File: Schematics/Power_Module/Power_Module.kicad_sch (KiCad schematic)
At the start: 131 parts, among them J1 ScrewSwitch B, J2 ScrewSwitch A, J3 Battery A, J4 USB_C_Female_USB2_Small, J5 Battery B, J6 Stack Male Edge Connector, J7 SWD_B, J8 SWD_B, Q1 AO4447A, Q2 AO4447A, U1 LMR51430XDDCR, U10 ISO1042BDWVR, U11 LM66100DCKR, U12 LM66100DCKR, U13 LM66100DCKR, U14 LM66100DCKR, U15 LM66100DCKR, U16 SCM3721ASA, U2 LMR51430XDDCR, U3 LMR51430XDDCR, U4 STM32F103C8Tx, U5 STM32F103C8Tx, U6 ACS37041KLHBLT-010B3, U7 ACS37041KLHBLT-010B3, U8 ACS37041KLHBLT-010B3, U9 AMS1117-3.3, Y1 X322516MMB4SI

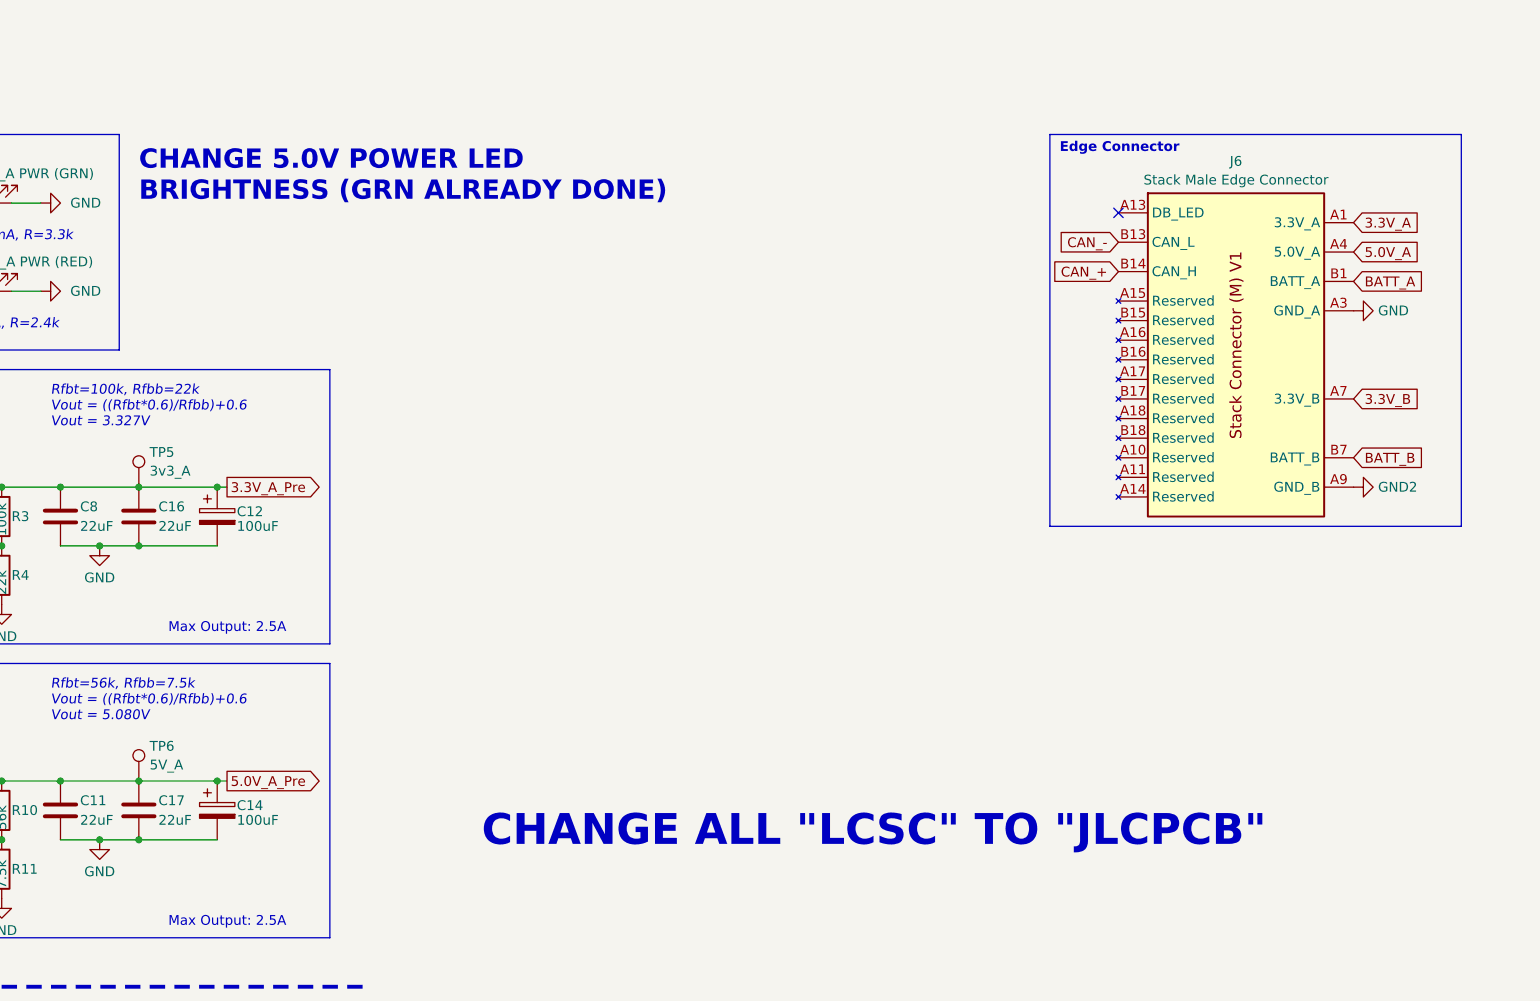
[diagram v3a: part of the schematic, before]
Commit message: Changed "LCSC" fields to "JLCPCB"
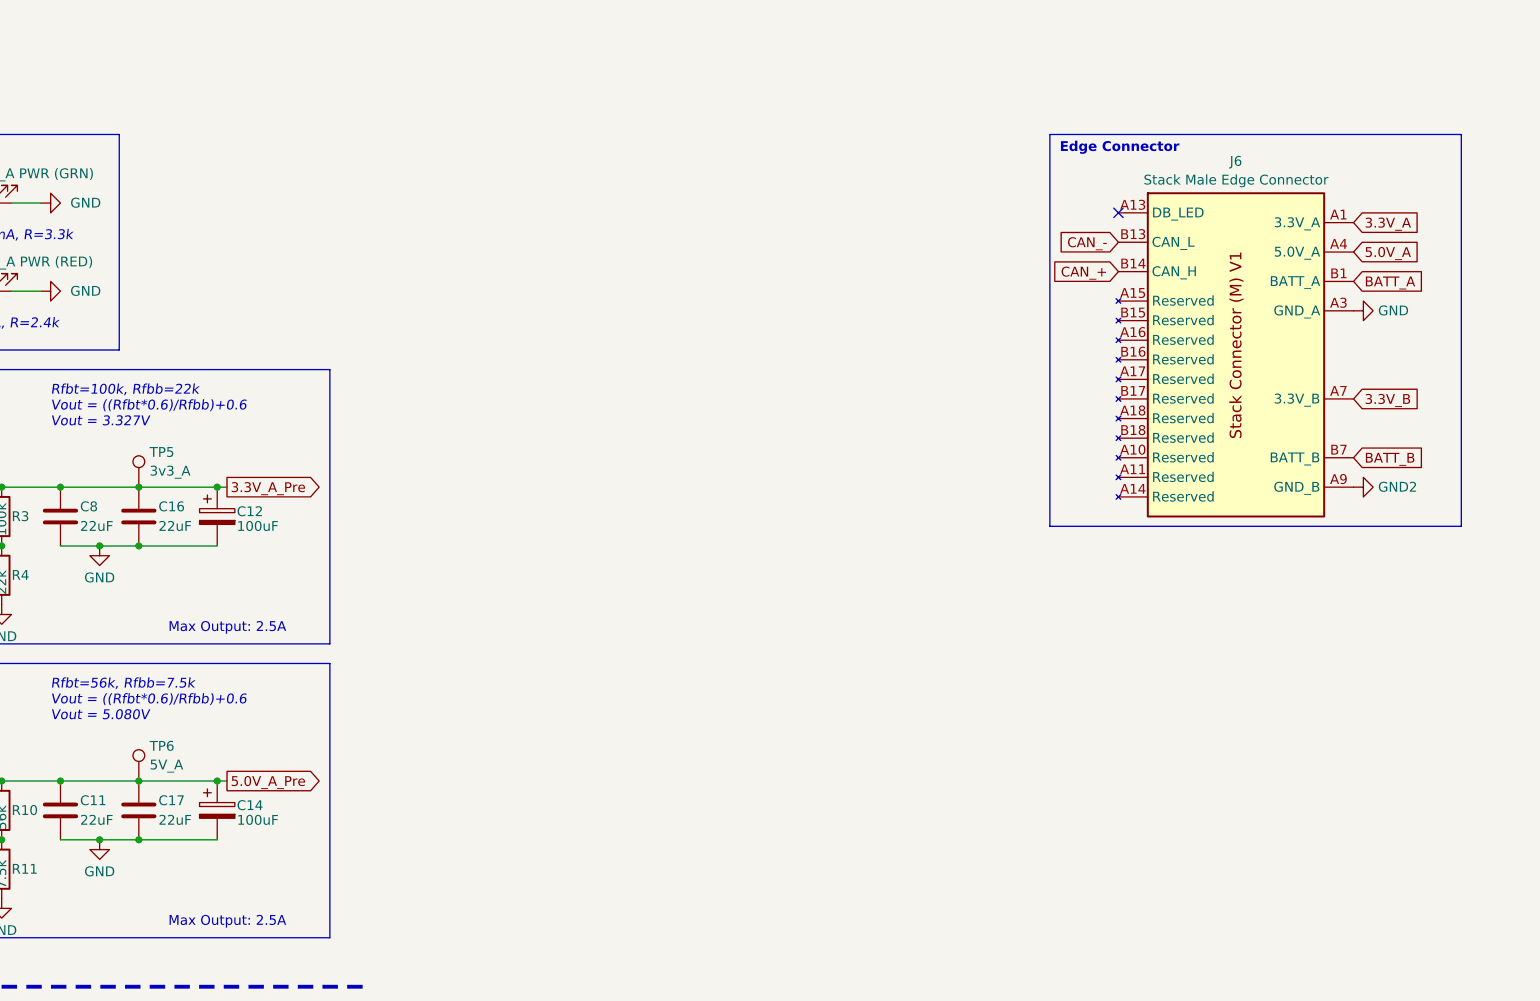
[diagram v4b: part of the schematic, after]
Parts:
- C1, C2, C3: JLCPCB (none) -> C1779; LCSC C1779 -> (none)
- C10, C21, C22, C4, C44, C45, C46, C47, C48, C49, C5, C50, C6, C7, C9: JLCPCB (none) -> C14663; LCSC C14663 -> (none)
- C11, C13, C16, C17, C18, C8: JLCPCB (none) -> C45783; LCSC C45783 -> (none)
- C19, C20: JLCPCB (none) -> C96446; LCSC C96446 -> (none)
- C23, C24: JLCPCB (none) -> C1634; LCSC C1634 -> (none)
- C25, C26, C27, C28, C29, C30, C31, C32: JLCPCB (none) -> C1525; LCSC C1525 -> (none)
- C33, C36: JLCPCB (none) -> C57112; LCSC C57112 -> (none)
- C34, C35, C37, C38: JLCPCB (none) -> C28323; LCSC C28323 -> (none)
- C39, C40, C41, C42, C43: JLCPCB (none) -> C15849; LCSC C15849 -> (none)
- D1, D3: JLCPCB (none) -> C2297; LCSC C2297 -> (none)
- D2: JLCPCB (none) -> C84256; LCSC C84256 -> (none)
- D5, D8: JLCPCB (none) -> C72038; LCSC C72038 -> (none)
- FB1, FB2: JLCPCB (none) -> C1015; LCSC C1015 -> (none)
- J4: JLCPCB (none) -> C2936184; LCSC C2936184 -> (none)
- Q1, Q2: JLCPCB (none) -> C125867; LCSC C125867 -> (none)
- R1, R23, R25, R26, R28, R3: JLCPCB (none) -> C25803; LCSC C25803 -> (none)
- R10: JLCPCB (none) -> C23206; LCSC C23206 -> (none)
- R11: JLCPCB (none) -> C23234; LCSC C23234 -> (none)
- R12, R5: JLCPCB (none) -> C22984; LCSC C22984 -> (none)
- R13, R15, R21, R22, R6: JLCPCB (none) -> C25804; LCSC C25804 -> (none)
- R16: JLCPCB (none) -> C22843; LCSC C22843 -> (none)
- R17, R18: JLCPCB (none) -> C23186; LCSC C23186 -> (none)
- R19, R20: JLCPCB (none) -> C23228; LCSC C23228 -> (none)
- R2, R4: JLCPCB (none) -> C31850; LCSC C31850 -> (none)
- R7, R9: JLCPCB (none) -> C22978; LCSC C22978 -> (none)
- R8: JLCPCB (none) -> C22940; LCSC C22940 -> (none)
- U10: JLCPCB (none) -> C484409; LCSC C484409 -> (none)
- U11, U12, U13, U14, U15: JLCPCB (none) -> C2869734; LCSC C2869734 -> (none)
- U9: JLCPCB (none) -> C6186; LCSC C6186 -> (none)
- Y1: JLCPCB (none) -> C13738; LCSC C13738 -> (none)
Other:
- note removed: "CHANGE 5.0V POWER LED BRIGHTNESS (GRN ALREADY DONE)"
- note removed: "CHANGE ALL "LCSC" TO "JLCPCB""

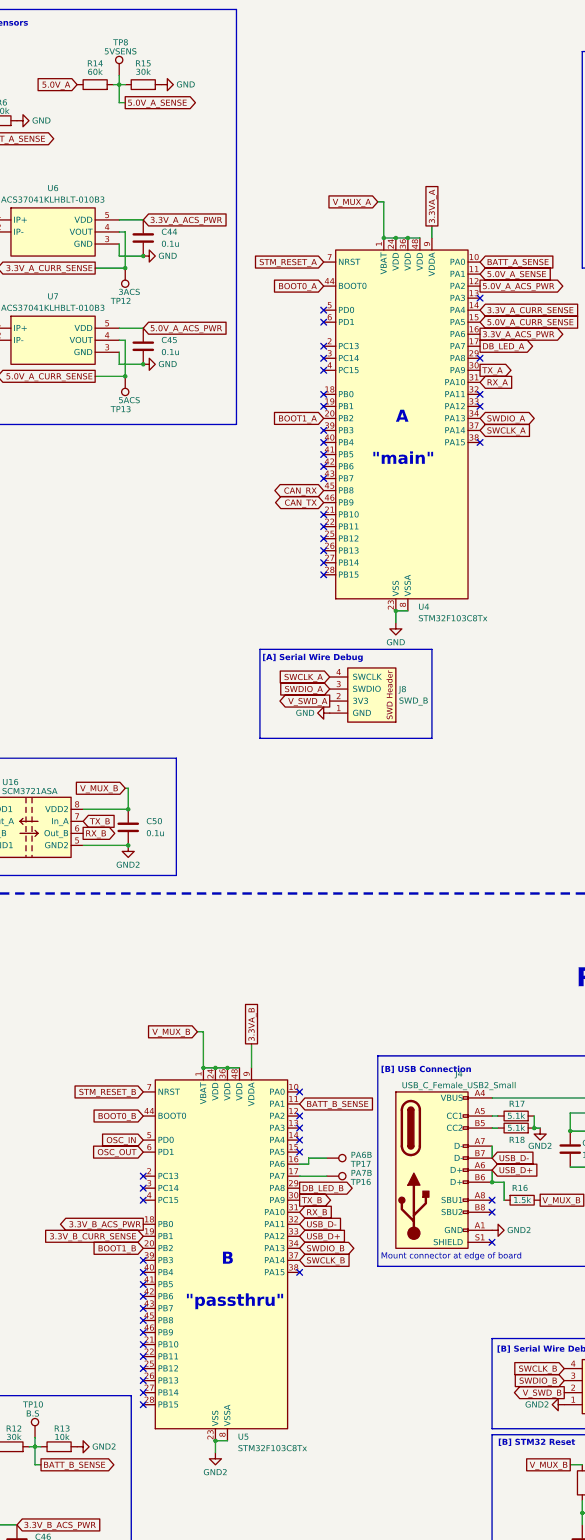
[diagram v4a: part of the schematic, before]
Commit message: Added/fixed part numbers
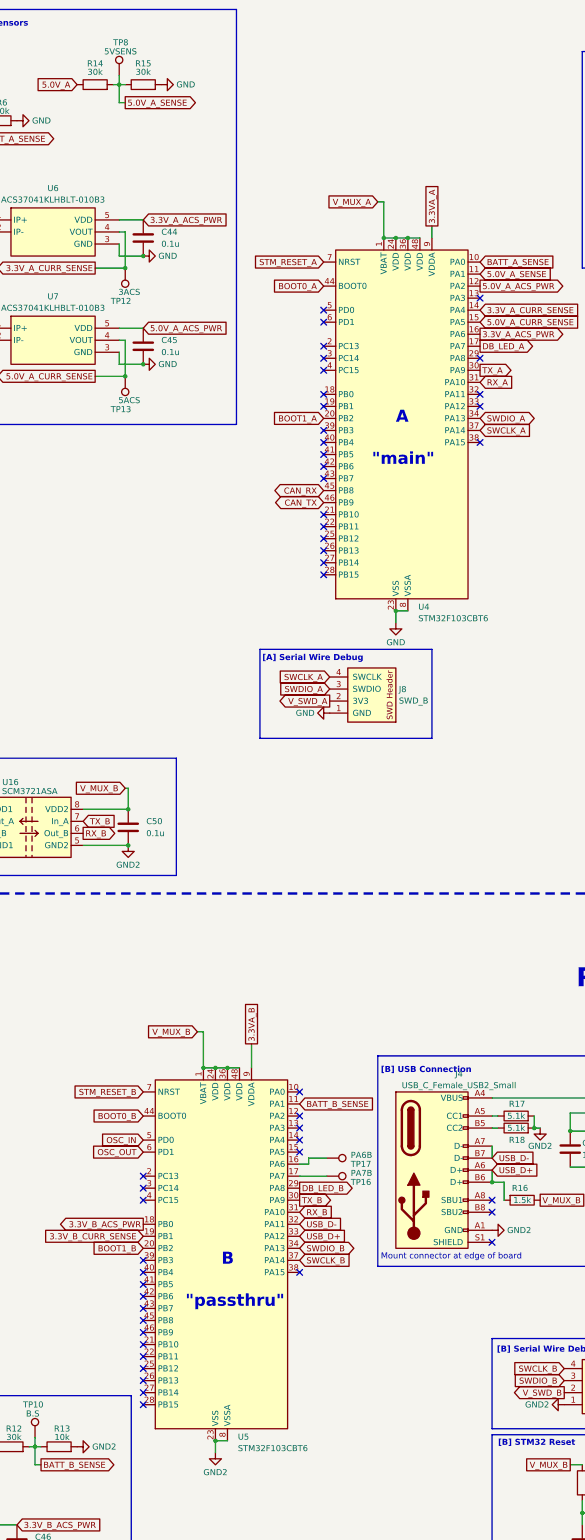
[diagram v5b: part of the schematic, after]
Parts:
- R14: value 60k -> 30k; JLCPCB (none) -> C22984
- R15: JLCPCB C25804 -> C22984
- U16: Digikey (none) -> 2725-SCM3721ASACT-ND
- U4, U5: value STM32F103C8Tx -> STM32F103CBT6; JLCPCB (none) -> C8304
- U6, U7, U8: Digikey (none) -> 620-ACS37041KLHBLT-010B3CT-ND
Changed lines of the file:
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@@
       (effects (font (size 1.27 1.27)) (justify left top) hide)
     )
+    (property "Digikey" "620-ACS37041KLHBLT-010B3CT-ND" (at 300.99 254 0)
+      (effects (font (size 1.27 1.27)) hide)
+    )
     (pin "1")
     (pin "2")
@@
       (effects (font (size 1.27 1.27)) (justify left top) hide)
     )
+    (property "Digikey" "620-ACS37041KLHBLT-010B3CT-ND" (at 327.66 1.27 0)
+      (effects (font (size 1.27 1.27)) hide)
+    )
     (pin "1")
     (pin "2")
@@
       (effects (font (size 1.27 1.27)) hide)
     )
-    (property "JLCPCB" "C25804" (at 360.68 -50.165 90)
+    (property "JLCPCB" "C22984" (at 360.68 -50.165 90)
       (effects (font (size 1.27 1.27)) hide)
     )
@@
       (effects (font (size 1.27 1.27)) hide)
     )
+    (property "Digikey" "2725-SCM3721ASACT-ND" (at 336.55 99.06 0)
+      (effects (font (size 1.27 1.27)) hide)
+    )
     (pin "1")
     (pin "2")
@@
       (effects (font (size 1.27 1.27)) (justify left))
     )
-    (property "Value" "STM32F103C8Tx" (at 380.6541 237.8243 0)
+    (property "Value" "STM32F103CBT6" (at 380.6541 237.8243 0)
       (effects (font (size 1.27 1.27)) (justify left))
     )
@@
       (effects (font (size 1.27 1.27)) hide)
     )
+    (property "JLCPCB" "C8304" (at 375.92 198.12 0)
+      (effects (font (size 1.27 1.27)) hide)
+    )
     (pin "1")
     (pin "10")
@@
       (effects (font (size 1.27 1.27)) (justify left top) hide)
     )
+    (property "Digikey" "620-ACS37041KLHBLT-010B3CT-ND" (at 327.66 -21.59 0)
+      (effects (font (size 1.27 1.27)) hide)
+    )
     (pin "1")
     (pin "2")
@@
       (effects (font (size 1.27 1.27)) (justify left))
     )
-    (property "Value" "STM32F103C8Tx" (at 418.7541 62.5643 0)
+    (property "Value" "STM32F103CBT6" (at 418.7541 62.5643 0)
       (effects (font (size 1.27 1.27)) (justify left))
     )
@@
       (effects (font (size 1.27 1.27)) hide)
     )
+    (property "JLCPCB" "C8304" (at 414.02 22.86 0)
+      (effects (font (size 1.27 1.27)) hide)
+    )
     (pin "1")
     (pin "10")
@@
       (effects (font (size 1.27 1.27)))
     )
-    (property "Value" "60k" (at 350.52 -52.8208 90)
+    (property "Value" "30k" (at 350.52 -52.8208 90)
       (effects (font (size 1.27 1.27)))
     )
@@
       (effects (font (size 1.27 1.27)) hide)
     )
-    (property "JLCPCB" "" (at 350.52 -50.165 90)
+    (property "JLCPCB" "C22984" (at 350.52 -50.165 90)
       (effects (font (size 1.27 1.27)) hide)
     )

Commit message: Tweaked some part numbers
-Changed STM32F103CB to STM32F103C8
-Changed USB port to C5178541
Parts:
- J4: JLCPCB C2936184 -> C5178541
- U4, U5: value STM32F103CBT6 -> STM32F103C8T6; JLCPCB C8304 -> C8734
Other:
- note removed: "DONT BE AFRAID TO MOUNT STUFF ON BOTTOM LAYER, SO LONG AS ITS MANUALLY INSTALLED"
- note removed: "This module is already going to be very different from a standard module. It does not have to be as user-friendly; it already doesn't have reset/boot buttons. Maybe remove most LMR66100s and only add ones to prevent it from back-powering the entire stack."
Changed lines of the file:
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@@
     (effects (font (size 4 4) (thickness 0.8) bold) (justify left bottom))
   )
-  (text "This module is already going to be\nvery different from a standard\nmodule. It does not have to be\nas user-friendly; it already doesn't\nhave reset/boot buttons.\n\nMaybe remove most LMR66100s and only\nadd ones to prevent it from back-powering\nthe entire stack."
-    (at 571.5 306.705 0)
-    (effects (font (size 4 4) (thickness 0.8) bold) (justify left bottom))
-  )
   (text "[B] STM32 Decoupling Capacitors for VBAT/VDD" (at 485.14 203.835 0)
     (effects (font (size 1.27 1.27) (thickness 0.254) bold) (justify left bottom))
@@
     (effects (font (size 1.27 1.27) (thickness 0.254) bold) (justify left bottom))
   )
-  (text "DONT BE AFRAID TO MOUNT STUFF ON BOTTOM\nLAYER, SO LONG AS ITS MANUALLY INSTALLED"
-    (at 262.89 299.085 0)
-    (effects (font (size 4 4) (thickness 0.8) bold) (justify left bottom))
-  )
   (text "FOLLOW LAYOUT EXAMPLE (9.4.2) FROM DATASHEET\nLMR51430: PFM @ 500kHz (simpler routing & higher efficiency)"
     (at 15.24 194.31 0)
@@
       (effects (font (size 1.27 1.27)) (justify left))
     )
-    (property "Value" "STM32F103CBT6" (at 380.6541 237.8243 0)
+    (property "Value" "STM32F103C8T6" (at 380.6541 237.8243 0)
       (effects (font (size 1.27 1.27)) (justify left))
     )
@@
       (effects (font (size 1.27 1.27)) hide)
     )
-    (property "JLCPCB" "C8304" (at 375.92 198.12 0)
+    (property "JLCPCB" "C8734" (at 375.92 198.12 0)
       (effects (font (size 1.27 1.27)) hide)
     )
@@
       (effects (font (size 1.27 1.27)) (justify left))
     )
-    (property "Value" "STM32F103CBT6" (at 418.7541 62.5643 0)
+    (property "Value" "STM32F103C8T6" (at 418.7541 62.5643 0)
       (effects (font (size 1.27 1.27)) (justify left))
     )
@@
       (effects (font (size 1.27 1.27)) hide)
     )
-    (property "JLCPCB" "C8304" (at 414.02 22.86 0)
+    (property "JLCPCB" "C8734" (at 414.02 22.86 0)
       (effects (font (size 1.27 1.27)) hide)
     )
@@
       (effects (font (size 1.27 1.27)) hide)
     )
-    (property "JLCPCB" "C2936184" (at 419.1 180.34 0)
+    (property "JLCPCB" "C5178541" (at 419.1 180.34 0)
       (effects (font (size 1.27 1.27)) hide)
     )
